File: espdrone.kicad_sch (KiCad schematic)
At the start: 50 parts, among them J5 Conn_01x04_Pin, SW1 SW_Push, U11 W25Q128JVP, U4 USBLC6-2P6, Y1 Crystal_GND24

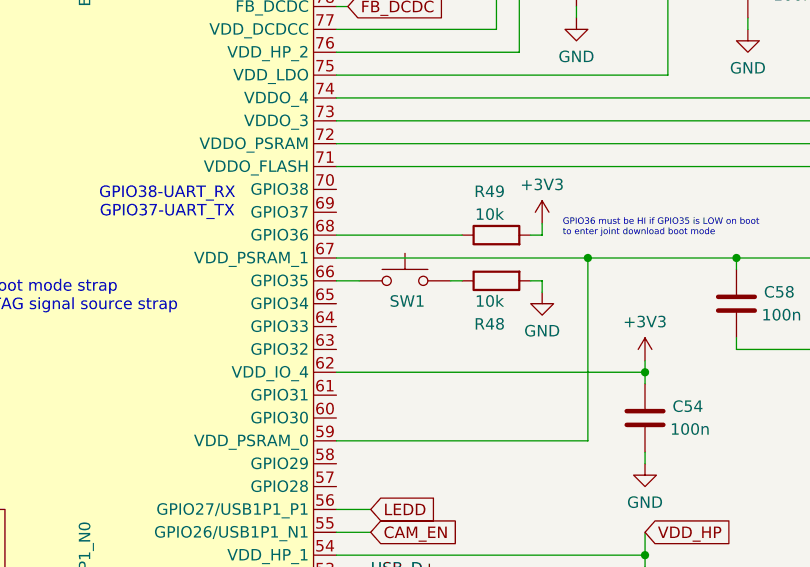
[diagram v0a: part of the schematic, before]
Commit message: Replace all switches with jumpers and fix some footprints
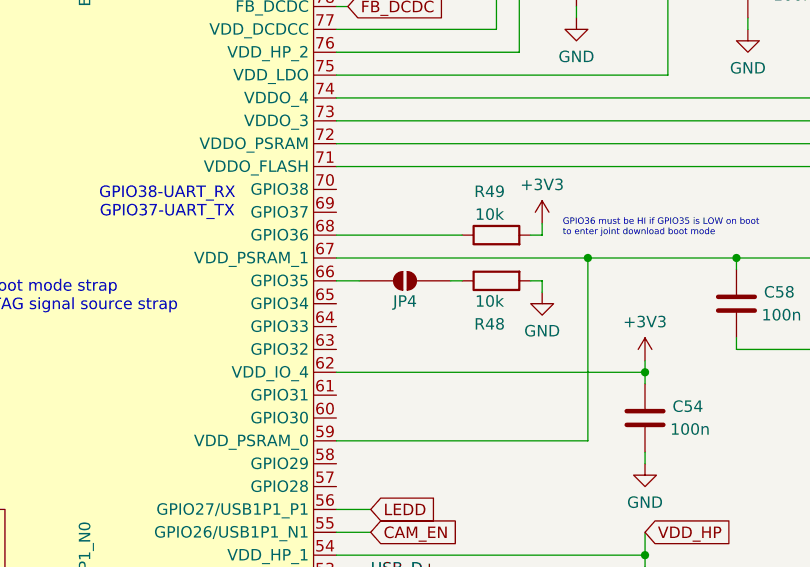
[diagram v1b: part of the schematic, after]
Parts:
- removed SW1: SW_Push, symbol Switch:SW_Push
- added JP4: SolderJumper_2_Open, Jumper:SolderJumper-2_P1.3mm_Open_RoundedPad1.0x1.5mm, symbol Jumper:SolderJumper_2_Open
- USB1: footprint easyeda2kicad:USB-C-SMD_TYPE-C-6PIN-2MD-073 -> easyeda2kicad:USB-C-SMD_TYPE-C-16PIN-2MD-073
- Y1: footprint (none) -> Crystal:Crystal_SMD_2016-4Pin_2.0x1.6mm
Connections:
- net at U9.66 (GPIO35): now also JP4.1 (A)
- net at R48.1: now also JP4.2 (B)
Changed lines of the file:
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@@
 	)
 	(symbol
+		(lib_id "Jumper:SolderJumper_2_Open")
+		(at 207.01 175.26 0)
+		(unit 1)
+		(body_style 1)
+		(exclude_from_sim no)
+		(in_bom no)
+		(on_board yes)
+		(in_pos_files yes)
+		(dnp no)
+		(property "Reference" "JP4"
+			(at 207.01 177.546 0)
+			(show_name no)
+			(do_not_autoplace no)
+			(effects
+				(font
+					(size 1.27 1.27)
+				)
+			)
+		)
+		(property "Value" "SolderJumper_2_Open"
+			(at 207.01 171.45 0)
+			(hide yes)
+			(show_name no)
+			(do_not_autoplace no)
+			(effects
+				(font
+					(size 1.27 1.27)
+				)
+			)
+		)
+		(property "Footprint" "Jumper:SolderJumper-2_P1.3mm_Open_RoundedPad1.0x1.5mm"
+			(at 207.01 175.26 0)
+			(hide yes)
+			(show_name no)
+			(do_not_autoplace no)
+			(effects
+				(font
+					(size 1.27 1.27)
+				)
+			)
+		)
+		(property "Datasheet" ""
+			(at 207.01 182.88 0)
+			(hide yes)
+			(show_name no)
+			(do_not_autoplace no)
+			(effects
+				(font
+					(size 1.27 1.27)
+				)
+			)
+		)
+		(property "Description" "Solder Jumper, 2-pole, open"
+			(at 207.01 180.34 0)
+			(hide yes)
+			(show_name no)
+			(do_not_autoplace no)
+			(effects
+				(font
+					(size 1.27 1.27)
+				)
+			)
+		)
+		(pin "2"
+		)
+		(pin "1"
+		)
+		(instances
+			(project "espdrone"
+				(path "/6e047eb1-70b3-49d8-916c-92a2df32e839"
+					(reference "JP4")
+					(unit 1)
+				)
+			)
+		)
+	)
+	(symbol
 		(lib_id "Device:C")
 		(at 85.09 107.95 0)
@@
 			)
 		)
-		(property "Footprint" ""
+		(property "Footprint" "Crystal:Crystal_SMD_2016-4Pin_2.0x1.6mm"
 			(at 119.38 48.26 0)
 			(hide yes)
@@
 	)
 	(symbol
-		(lib_id "Switch:SW_Push")
-		(at 207.01 175.26 0)
-		(unit 1)
-		(body_style 1)
-		(exclude_from_sim no)
-		(in_bom yes)
-		(on_board yes)
-		(in_pos_files yes)
-		(dnp no)
-		(property "Reference" "SW1"
-			(at 207.264 177.546 0)
-			(show_name no)
-			(do_not_autoplace no)
-			(effects
-				(font
-					(size 1.27 1.27)
-				)
-			)
-		)
-		(property "Value" "SW_Push"
-			(at 207.01 170.18 0)
-			(hide yes)
-			(show_name no)
-			(do_not_autoplace no)
-			(effects
-				(font
-					(size 1.27 1.27)
-				)
-			)
-		)
-		(property "Footprint" ""
-			(at 207.01 170.18 0)
-			(hide yes)
-			(show_name no)
-			(do_not_autoplace no)
-			(effects
-				(font
-					(size 1.27 1.27)
-				)
-			)
-		)
-		(property "Datasheet" ""
-			(at 207.01 170.18 0)
-			(hide yes)
-			(show_name no)
-			(do_not_autoplace no)
-			(effects
-				(font
-					(size 1.27 1.27)
-				)
-			)
-		)
-		(property "Description" "Push button switch, generic, two pins"
-			(at 207.01 175.26 0)
-			(hide yes)
-			(show_name no)
-			(do_not_autoplace no)
-			(effects
-				(font
-					(size 1.27 1.27)
-				)
-			)
-		)
-		(pin "1"
-		)
-		(pin "2"
-		)
-		(instances
-			(project "espdrone"
-				(path "/6e047eb1-70b3-49d8-916c-92a2df32e839"
-					(reference "SW1")
-					(unit 1)
-				)
-			)
-		)
-	)
-	(symbol
 		(lib_id "power:GND")
 		(at 205.74 125.73 0)
@@
 			)
 		)
-		(property "Footprint" "easyeda2kicad:USB-C-SMD_TYPE-C-6PIN-2MD-073"
+		(property "Footprint" "easyeda2kicad:USB-C-SMD_TYPE-C-16PIN-2MD-073"
 			(at 274.32 81.28 0)
 			(hide yes)

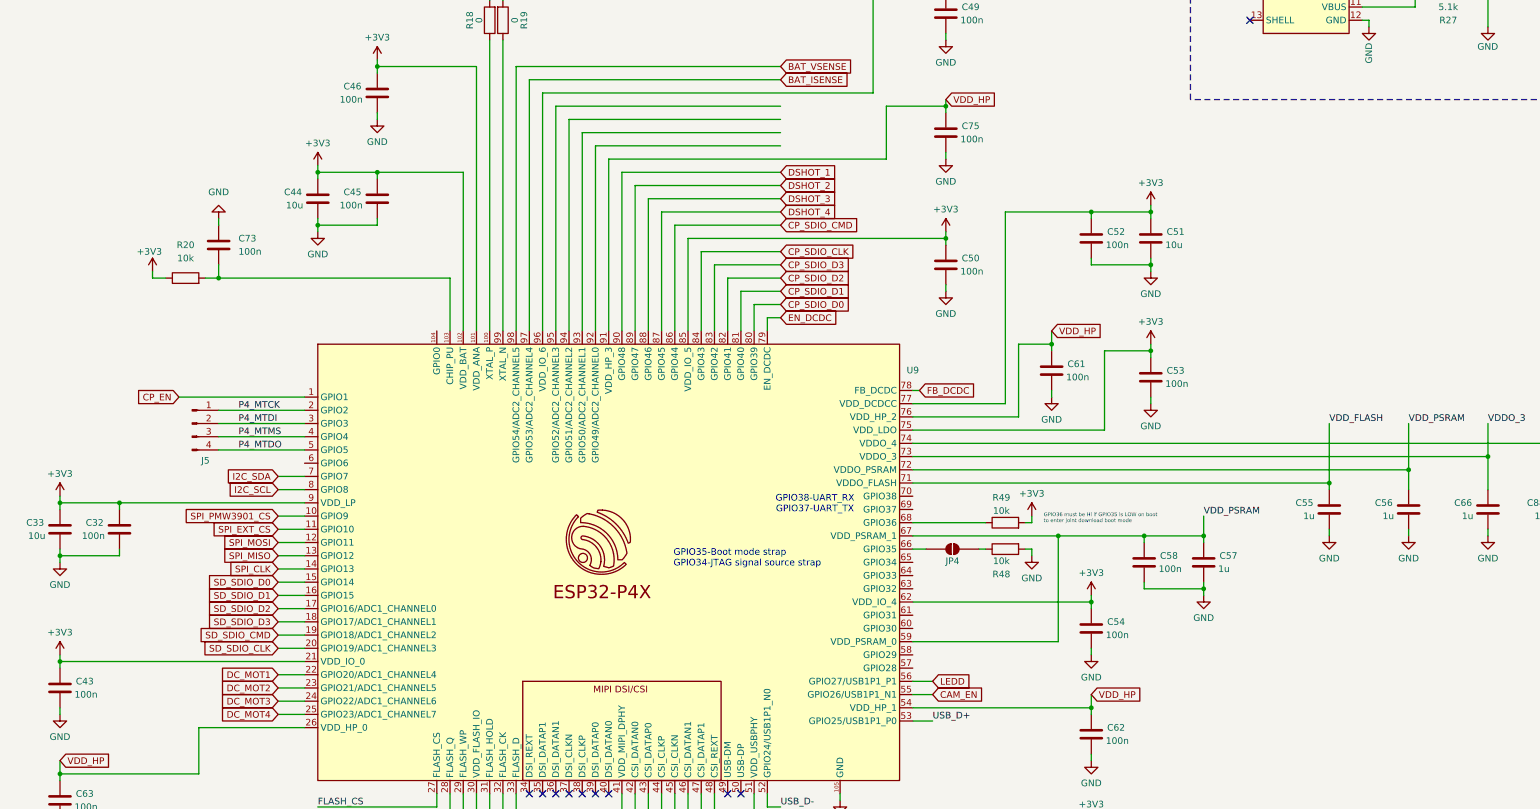
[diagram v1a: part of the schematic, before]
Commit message: Improve connectors and DC flyback diode
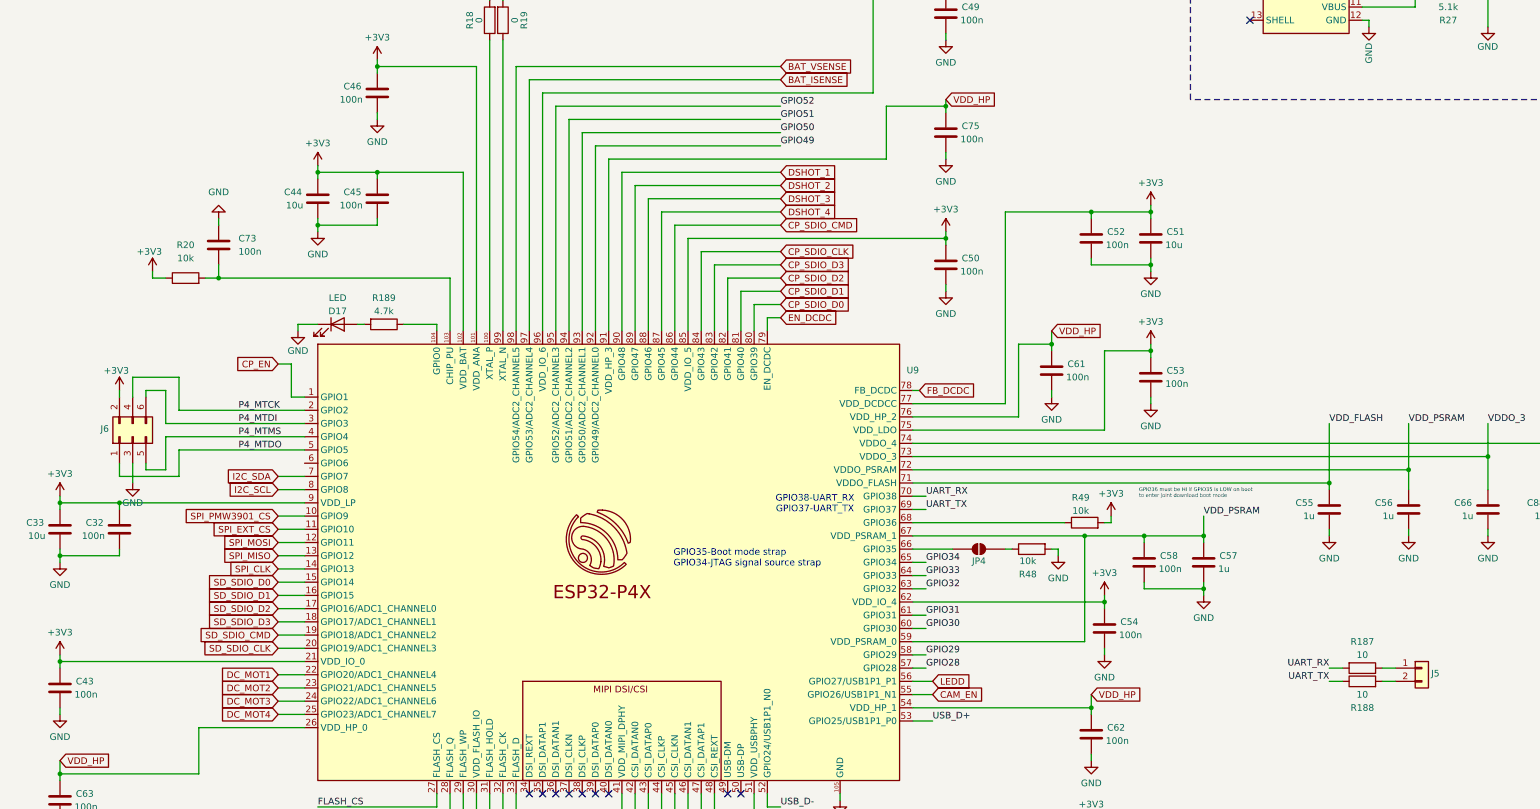
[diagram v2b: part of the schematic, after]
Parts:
- removed J5: Conn_01x04_Pin, symbol Connector:Conn_01x04_Pin
- added D17: LED, LED_SMD:LED_0402_1005Metric, symbol Device:LED
- added J5: Conn_01x02, symbol Connector_Generic:Conn_01x02
- added J6: Conn_02x03_Odd_Even, symbol Connector_Generic:Conn_02x03_Odd_Even
- added R187, R188: 10, Resistor_SMD:R_0603_1608Metric, symbol Device:R
- added R189: 4.7k, Resistor_SMD:R_0603_1608Metric, symbol Device:R
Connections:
- net +3V3: now also J6.2 (Pin_2)
- net GND: now also D17.1 (K), J6.3 (Pin_3)
- net P4_MTCK: now also J6.4 (Pin_4)
- net P4_MTDI: now also J6.6 (Pin_6)
- net P4_MTDO: now also J6.1 (Pin_1)
- net P4_MTMS: now also J6.5 (Pin_5)
- net at U9.104 (GPIO0): now also R189.1
- net GPIO28: now reaches U9.57 (GPIO28)
- net GPIO29: now reaches U9.58 (GPIO29)
- net GPIO30: now reaches U9.60 (GPIO30)
- net GPIO31: now reaches U9.61 (GPIO31)
- net GPIO32: now reaches U9.63 (GPIO32)
- net GPIO33: now reaches U9.64 (GPIO33)
- net GPIO34: now reaches U9.65 (GPIO34)
- net UART_TX: now reaches U9.69 (GPIO37)
- net UART_TX: now also R188.1
- net UART_RX: now reaches U9.70 (GPIO38)
- net UART_RX: now also R187.2
- net GPIO49: now reaches U9.92 (GPIO49/ADC2_CHANNEL0)
- net GPIO50: now reaches U9.93 (GPIO50/ADC2_CHANNEL1)
- net GPIO51: now reaches U9.94 (GPIO51/ADC2_CHANNEL2)
- net GPIO52: now reaches U9.95 (GPIO52/ADC2_CHANNEL3)
- new net: J5.2 (Pin_2), R188.2
- new net: D17.2 (A), R189.2
- new net: J5.1 (Pin_1), R187.1
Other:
- moved on the sheet: C54, JP4, R48, R49

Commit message: Reset schematic part number annotations
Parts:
- renumbered C33 to C1, C45 to C10, C48 to C11, C47 to C12, C70 to C13, C71 to C14, C49 to C15, C75 to C16, C50 to C17, C72 to C18, C67 to C19, C43 to C2, C68 to C20, C61 to C21, C52 to C22, C62 to C23, C69 to C24, C54 to C25, C58 to C26, C51 to C27, C53 to C28, C57 to C29, C63 to C3, C55 to C30, C56 to C31, C66 to C32, C88 to C33, C74 to C34, C32 to C4, C65 to C5, C64 to C6, C73 to C7, C44 to C8, C46 to C9, D17 to D1, J6 to J1, J5 to J2, JP4 to JP1, R20 to R1, R26 to R10, R27 to R11, R23 to R12, R189 to R2, R18 to R3, R19 to R4, R29 to R5, R48 to R6, R49 to R7, R187 to R8, R188 to R9, U9 to U1, U4 to U2, U11 to U3

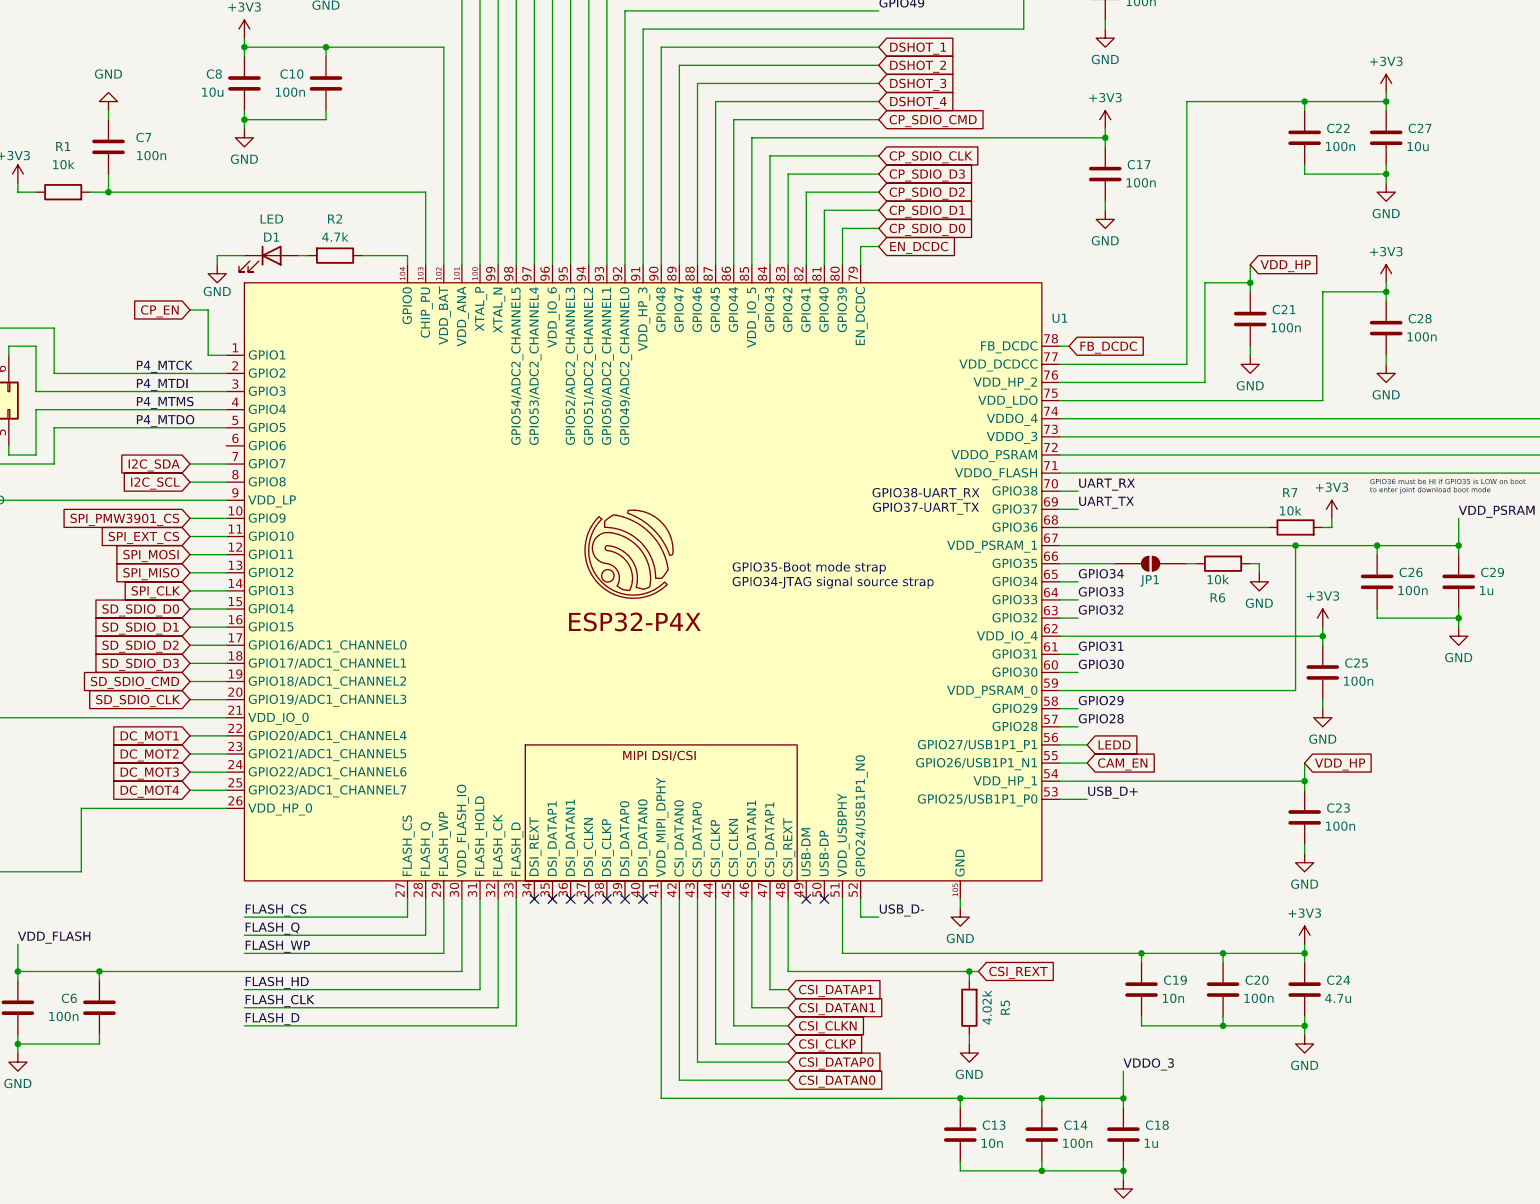
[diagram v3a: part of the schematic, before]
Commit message: Resize lots of passives and replace current resistors with 4-wire shunts
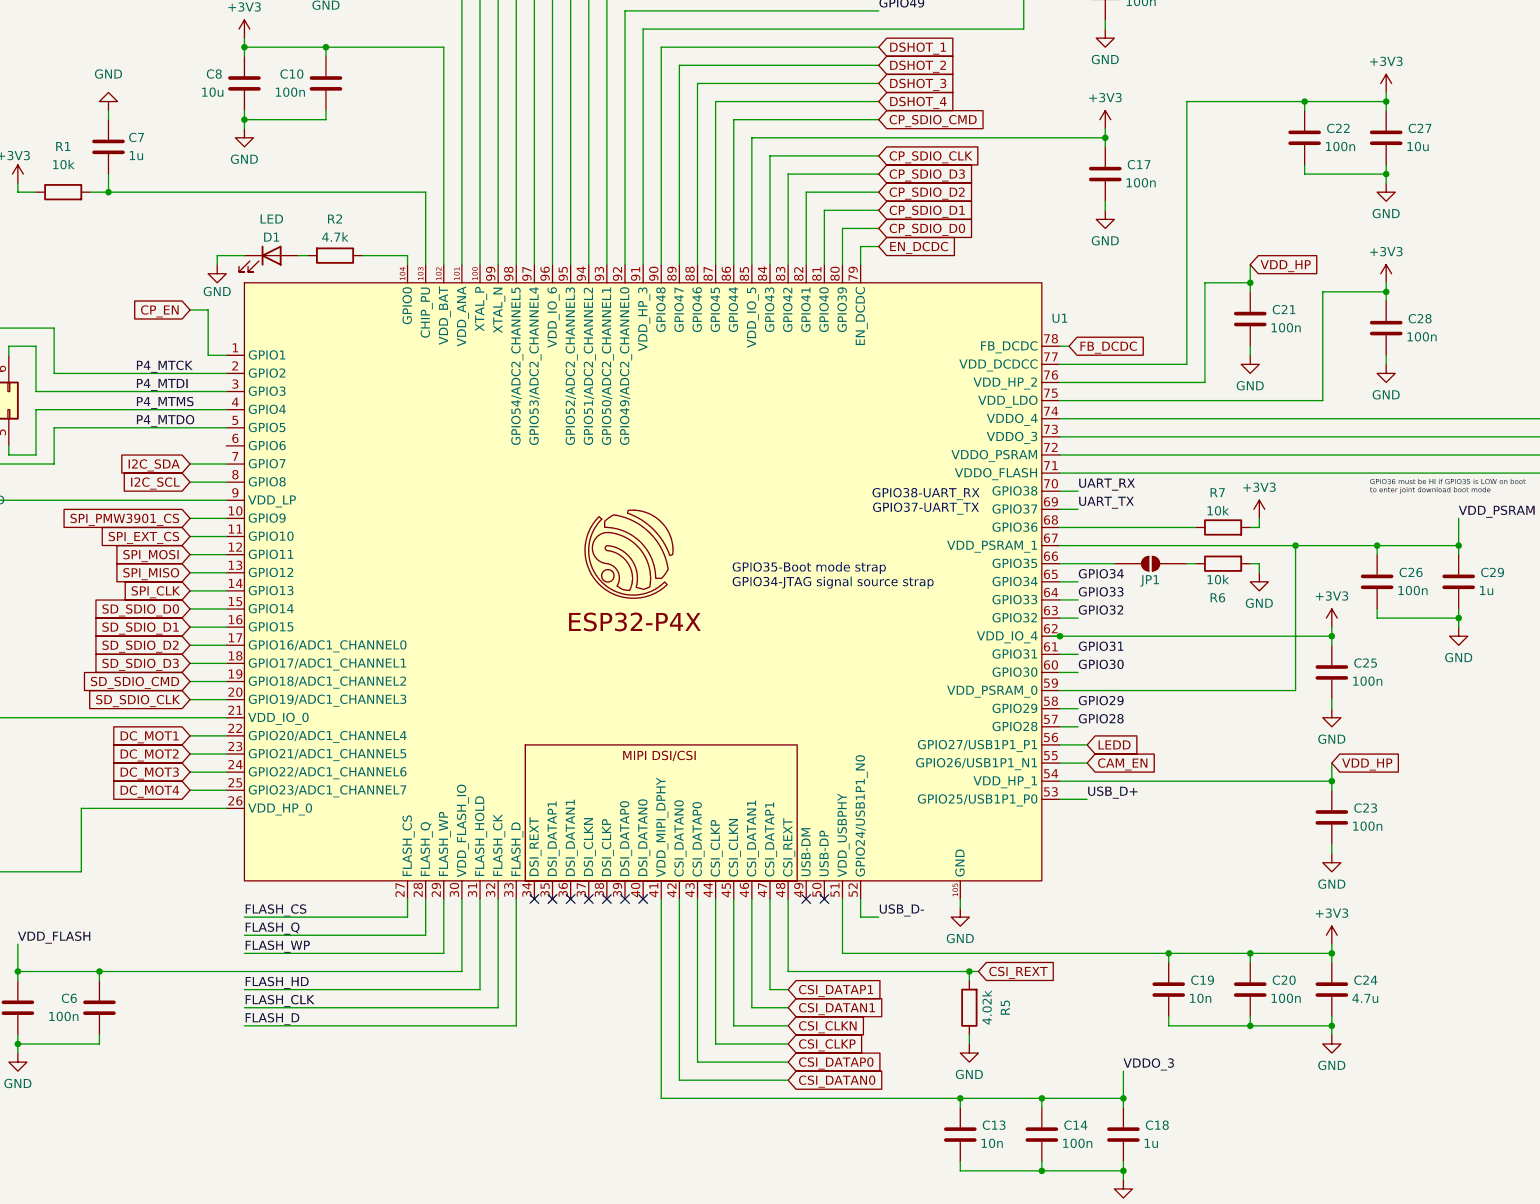
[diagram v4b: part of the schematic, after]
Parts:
- C1: footprint Capacitor_SMD:C_0603_1608Metric -> Capacitor_SMD:C_0805_2012Metric
- C10, C11, C12, C13, C14, C15, C16, C17, C18, C19, C2, C20, C21, C22, C23, C25, C26, C28, C3, C30, C31, C32, C33, C34, C4, C5, C6, C9: footprint Capacitor_SMD:C_0603_1608Metric -> Capacitor_SMD:C_0402_1005Metric
- C7: value 100n -> 1u
- J1: footprint (none) -> Connector_PinHeader_1.27mm:PinHeader_2x03_P1.27mm_Vertical
- J2: footprint (none) -> Connector_PinHeader_1.27mm:PinHeader_1x02_P1.27mm_Vertical
- R1, R10, R11, R12, R2, R3, R4, R5, R6, R7, R8, R9: footprint Resistor_SMD:R_0603_1608Metric -> Resistor_SMD:R_0402_1005Metric
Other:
- moved on the sheet: C19, C20, C23, C24, C25, R7

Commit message: Fix the orientation of most resistor annotations
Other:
- moved on the sheet: R10, R11, U2, USB1

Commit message: Fix ERC errors
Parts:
- added J12: Conn_01x14, Connector_PinHeader_1.27mm:PinHeader_2x07_P1.27mm_Vertical, symbol Connector_Generic:Conn_01x14
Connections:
- net +3V3: now also J12.1 (Pin_1)
- net GND: now also J12.14 (Pin_14)
- net GPIO28: now also J12.3 (Pin_3)
- net GPIO29: now also J12.4 (Pin_4)
- net GPIO30: now also J12.5 (Pin_5)
- net GPIO31: now also J12.6 (Pin_6)
- net GPIO32: now also J12.7 (Pin_7)
- net GPIO33: now also J12.8 (Pin_8)
- net GPIO34: now also J12.9 (Pin_9)
- net GPIO49: now also J12.10 (Pin_10)
- net GPIO50: now also J12.11 (Pin_11)
- net GPIO51: now also J12.12 (Pin_12)
- net GPIO52: now also J12.13 (Pin_13)
- net GPIO6: now reaches U1.6 (GPIO6)
- net GPIO6: now also J12.2 (Pin_2)
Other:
- note added: "UART breakout"
- note added: "Unused GPIO breakout"
- moved on the sheet: J2, R8, R9
